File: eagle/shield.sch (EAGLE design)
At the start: 31 parts, among them IC1 REG1117

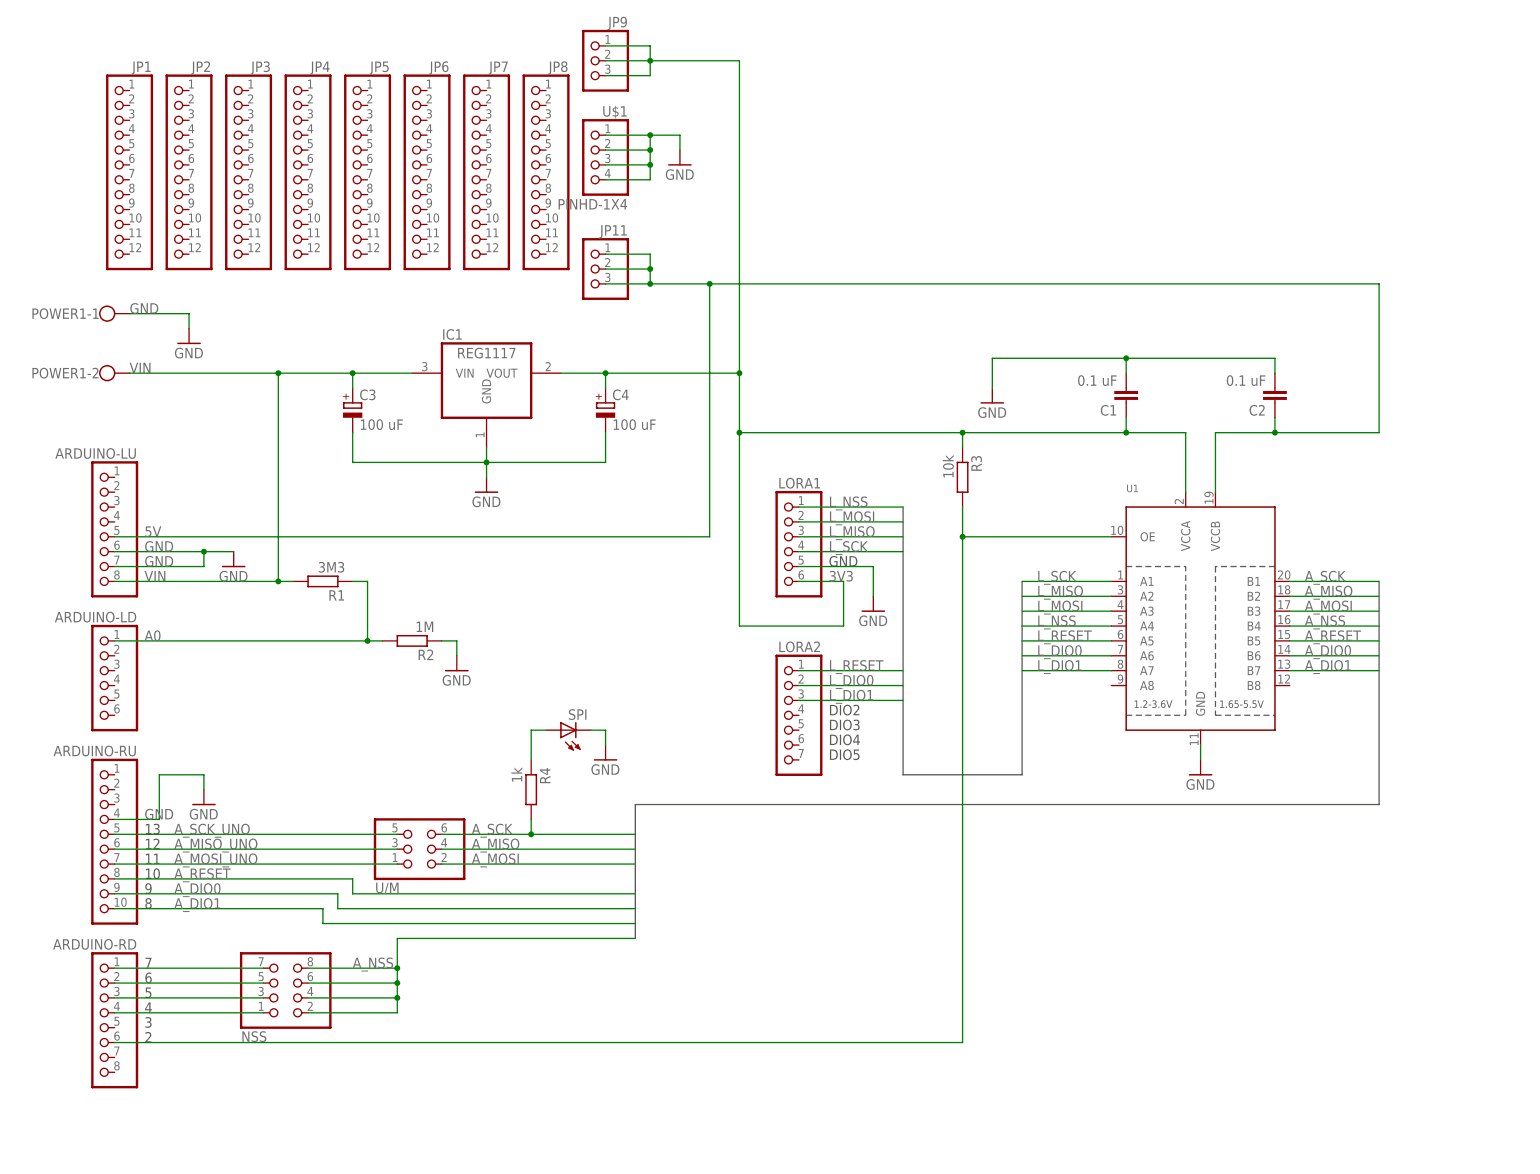
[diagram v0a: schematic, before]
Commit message: Shield layout update
Added two separate TXB0104 instead of one TXB0108 (signal direction issues), added EN solder jumper for LED, removed battery level measurement, increased the protoyping area size, general layout changes for easier soldering.
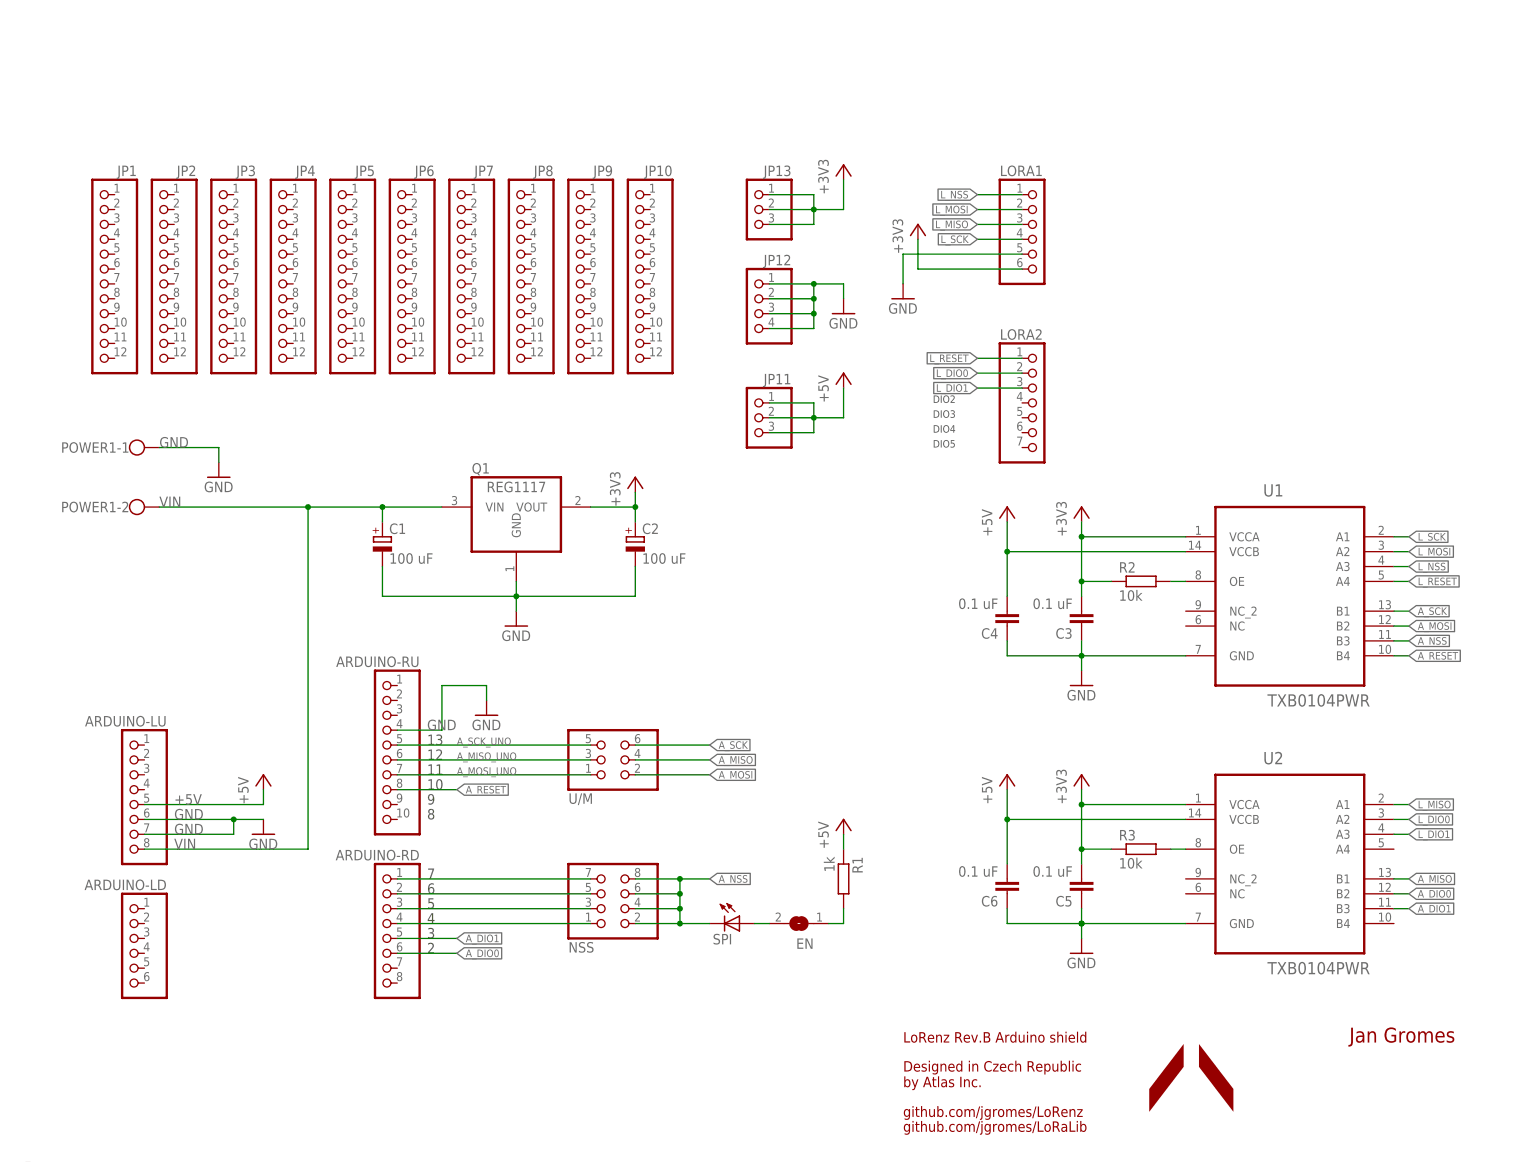
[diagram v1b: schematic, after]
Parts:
- removed IC1: REG1117, burr-brown:REG1117
- removed R4: 1k, rcl:R-EU_R0603
- removed U$1: PINHD-1X4, adafruit:PINHD-1X4
- added C5, C6: 0.1 uF, rcl:C-EUC0603
- added EN: (no value), jumper:SJ
- added JP10: (no value), adafruit:PINHD-1X12-CB
- added JP12: PINHD-1X4, adafruit:PINHD-1X4
- added JP13: (no value), adafruit:PINHD-1X3CB
- added Q1: REG1117, burr-brown:REG1117
- added U2: TXB0104PWR, Texas Instruments_By_element14_Batch_1:TXB0104PWR
- C1, C2: value 0.1 uF -> 100 uF; device rcl:C-EUC0603 -> rcl:CPOL-EUSMCD
- C3, C4: value 100 uF -> 0.1 uF; device rcl:CPOL-EUSMCD -> rcl:C-EUC0603
- JP9: device adafruit:PINHD-1X3CB -> adafruit:PINHD-1X12-CB
- R1: value 3M3 -> 1k
- R2: value 1M -> 10k
- U1: value (none) -> TXB0104PWR; device adafruit:TXB0108PWR -> Texas Instruments_By_element14_Batch_1:TXB0104PWR
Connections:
- removed net 3V3: C1.1, C4.+, IC1.VOUT, JP9.1, JP9.2, JP9.3, LORA1.6, R3.1, U1.VCCA
- removed net 5V: ARDUINO-LU.5, C2.1, JP11.1, JP11.2, JP11.3, U1.VCCB
- removed net A0: ARDUINO-LD.1, R1.1, R2.2
- removed net OE: ARDUINO-RD.6, R3.2, U1.OE
- new net +3V3: C2.+, C3.2, C5.2, JP13.1, JP13.2, JP13.3, LORA1.6, Q1.VOUT, R2.1, R3.1, U1.VCCA, U2.VCCA
- new net +5V: ARDUINO-LU.5, C4.2, C6.2, JP11.1, JP11.2, JP11.3, R1.1, U1.VCCB, U2.VCCB
- new net N$10: EN.1, R1.2
- new net N$11: R2.2, U1.OE
- new net N$12: R3.2, U2.OE
- net A_DIO0: now also ARDUINO-RD.6, U2.B2; no longer ARDUINO-RU.9, U1.B6
- net A_DIO1: now also ARDUINO-RD.5, U2.B3; no longer ARDUINO-RU.10, U1.B7
- net A_MISO: now also U2.B1; no longer U1.B2
- net A_MOSI: now also U1.B2; no longer U1.B3
- net A_NSS: now also SPI.C, U1.B3; no longer U1.B4
- net A_RESET: now also U1.B4; no longer U1.B5
- net A_SCK: no longer R4.2
- net GND: now also C1.-, C2.-, C3.1, C4.1, C5.1, C6.1, JP12.1, JP12.2, JP12.3, JP12.4, Q1.GND, U2.GND; no longer C1.2, C2.2, C3.-, C4.-, IC1.GND, R2.1, SPI.C, U$1.1, U$1.2, U$1.3, U$1.4
- net L_DIO0: now also U2.A2; no longer U1.A6
- net L_DIO1: now also U2.A3; no longer U1.A7
- net L_MISO: now also U2.A1; no longer U1.A2
- net L_MOSI: now also U1.A2; no longer U1.A3
- net L_NSS: now also U1.A3; no longer U1.A4
- net L_RESET: now also U1.A4; no longer U1.A5
- net N$4: now also EN.2; no longer R4.1
- net VIN: now also C1.+, Q1.VIN; no longer C3.+, IC1.VIN, R1.2
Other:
- note added: "C:/Users/Honza/Desktop/ATLAS/atlas_logo_notext_gs.bmp"
- note added: "Designed in Czech Republic by Atlas Inc."
- note added: "Jan Gromes"
- note added: "LoRenz Rev.B Arduino shield"
- note added: "github.com/jgromes/LoRaLib"
- note added: "github.com/jgromes/LoRenz"
- note removed: "GND"
- moved on the sheet: ARDUINO-LD, ARDUINO-LU, ARDUINO-RD, ARDUINO-RU, JP1, JP11, JP2, JP3, JP4, JP5, JP6, JP7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
